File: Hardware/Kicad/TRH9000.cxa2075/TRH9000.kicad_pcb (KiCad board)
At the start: 4 copper layers, 100 x 77.5 mm, 67 parts, among them J2 RGB, J3 Composite, J4 SVIDEO, Q1 BC817, U1 74HC138, U2 74HC32, U3 V9990, U4 KM428C256, U5 KM428C256, U6 CXA2075M, X1 14.31818MHz, Y1 21.47727Mhz

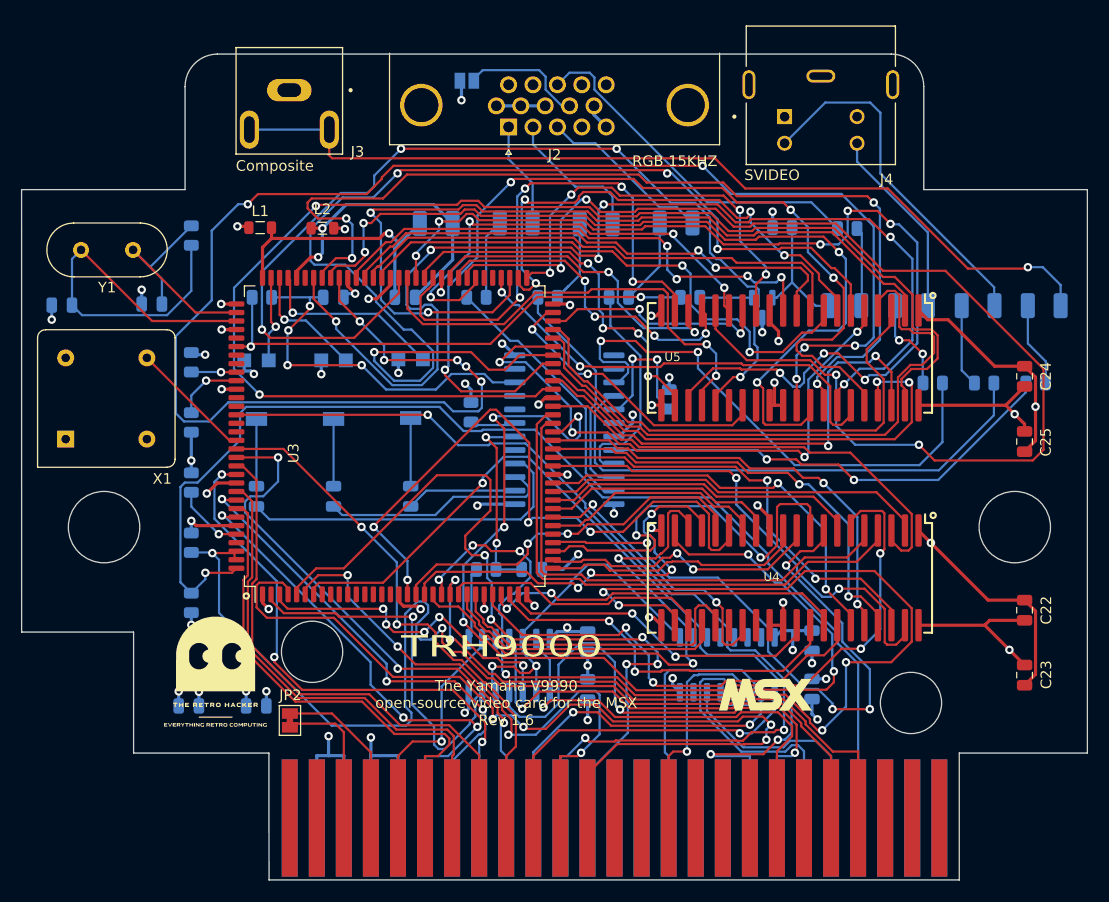
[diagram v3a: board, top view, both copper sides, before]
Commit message: kicad 8 migration. minor positioning for the connectors
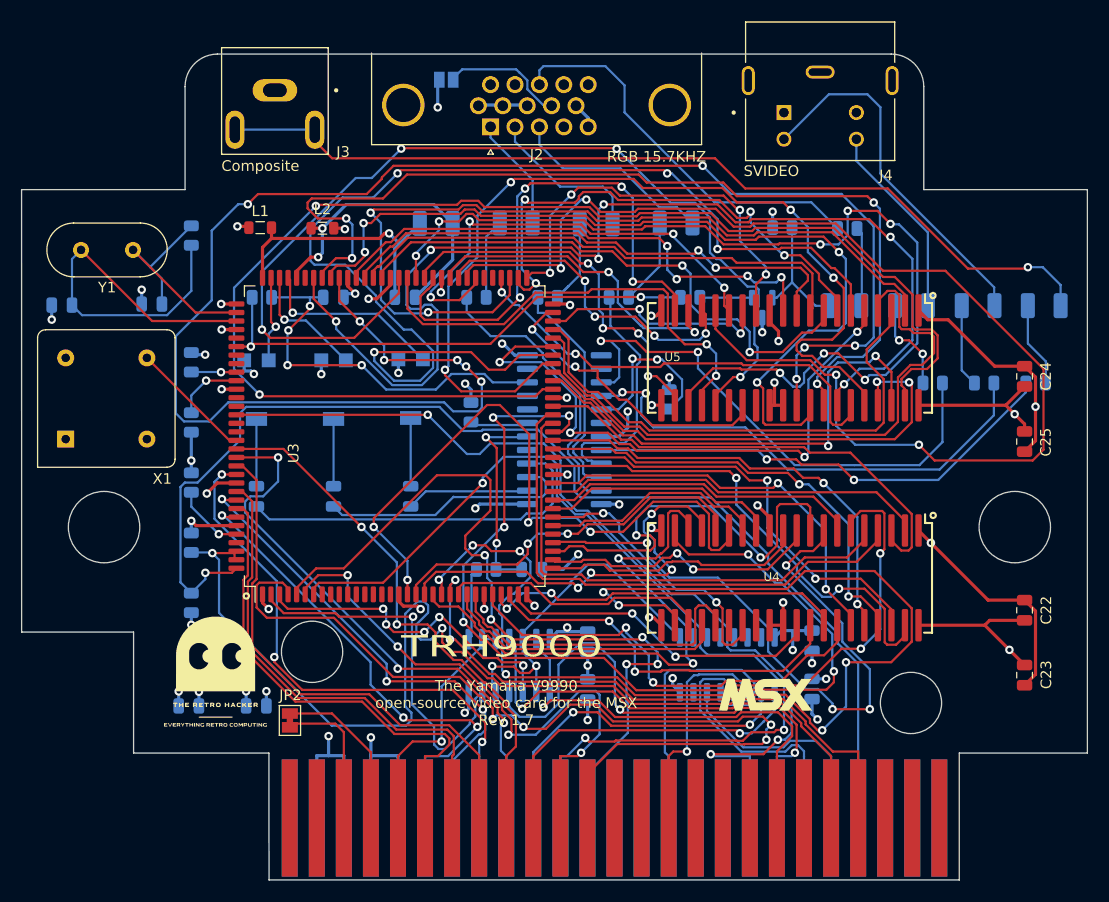
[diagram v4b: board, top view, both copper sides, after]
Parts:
- U6: footprint Package_SO:SOP-24_7.5x15.4mm_P1.27mm -> Package_SO:SO-24_5.3x15mm_P1.27mm
- moved JP1 1.94 mm to (141.3, 58.4)
- moved J2 1.69 mm to (145.4, 62.8)
- moved J3 1.35 mm to (125.2, 59.4)
- moved J4 0.39 mm to (176.4, 57.7)
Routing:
- net /VDP/V0S3: track 95.2 -> 90.9 mm
- net Net-(U6-YOUT): track 50.1 -> 46.1 mm, vias 0 -> 2
- net /VIDEO/CSYNCO: track 33.5 -> 37.3 mm
- net +5V: track 108.5 -> 111.2 mm
- net /VIDEO/BOUT: track 16.4 -> 19.1 mm
- net Net-(U6-YTRAP): track 13.2 -> 15.6 mm
- net Net-(U6-BIN): track 32.3 -> 34.6 mm
- net /~{RESET}: track 86.4 -> 88.8 mm
- net GND: track 117.4 -> 119.8 mm
- net Net-(U6-GIN): track 21.8 -> 24.1 mm
- net Net-(U6-ROUT): track 24.9 -> 27.0 mm
- net Net-(U6-BOUT): track 20.7 -> 22.6 mm
- net /A3: track 92.4 -> 94.1 mm
- net /VIDEO/GOUT: track 13.7 -> 15.3 mm
- net /VDP/V1S2: track 55.3 -> 56.8 mm
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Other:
- board text added: "RGB 15.7KHZ"
- board text added: "The Yamaha V9990 open-source video card for the MSX Rev ${REVISION}"
- board text removed: "RGB 15KHZ"
- board text removed: "The Yamaha V9990 open-source video card for the MSX Rev 1.6"
